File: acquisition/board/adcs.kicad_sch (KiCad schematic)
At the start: 111 parts, among them U1 AD9251, U2 XC7A50T-1FTG256C, U3 AD9251, U4 AD9251, U5 AD9251, U6 ICE40UP5K_QFN48

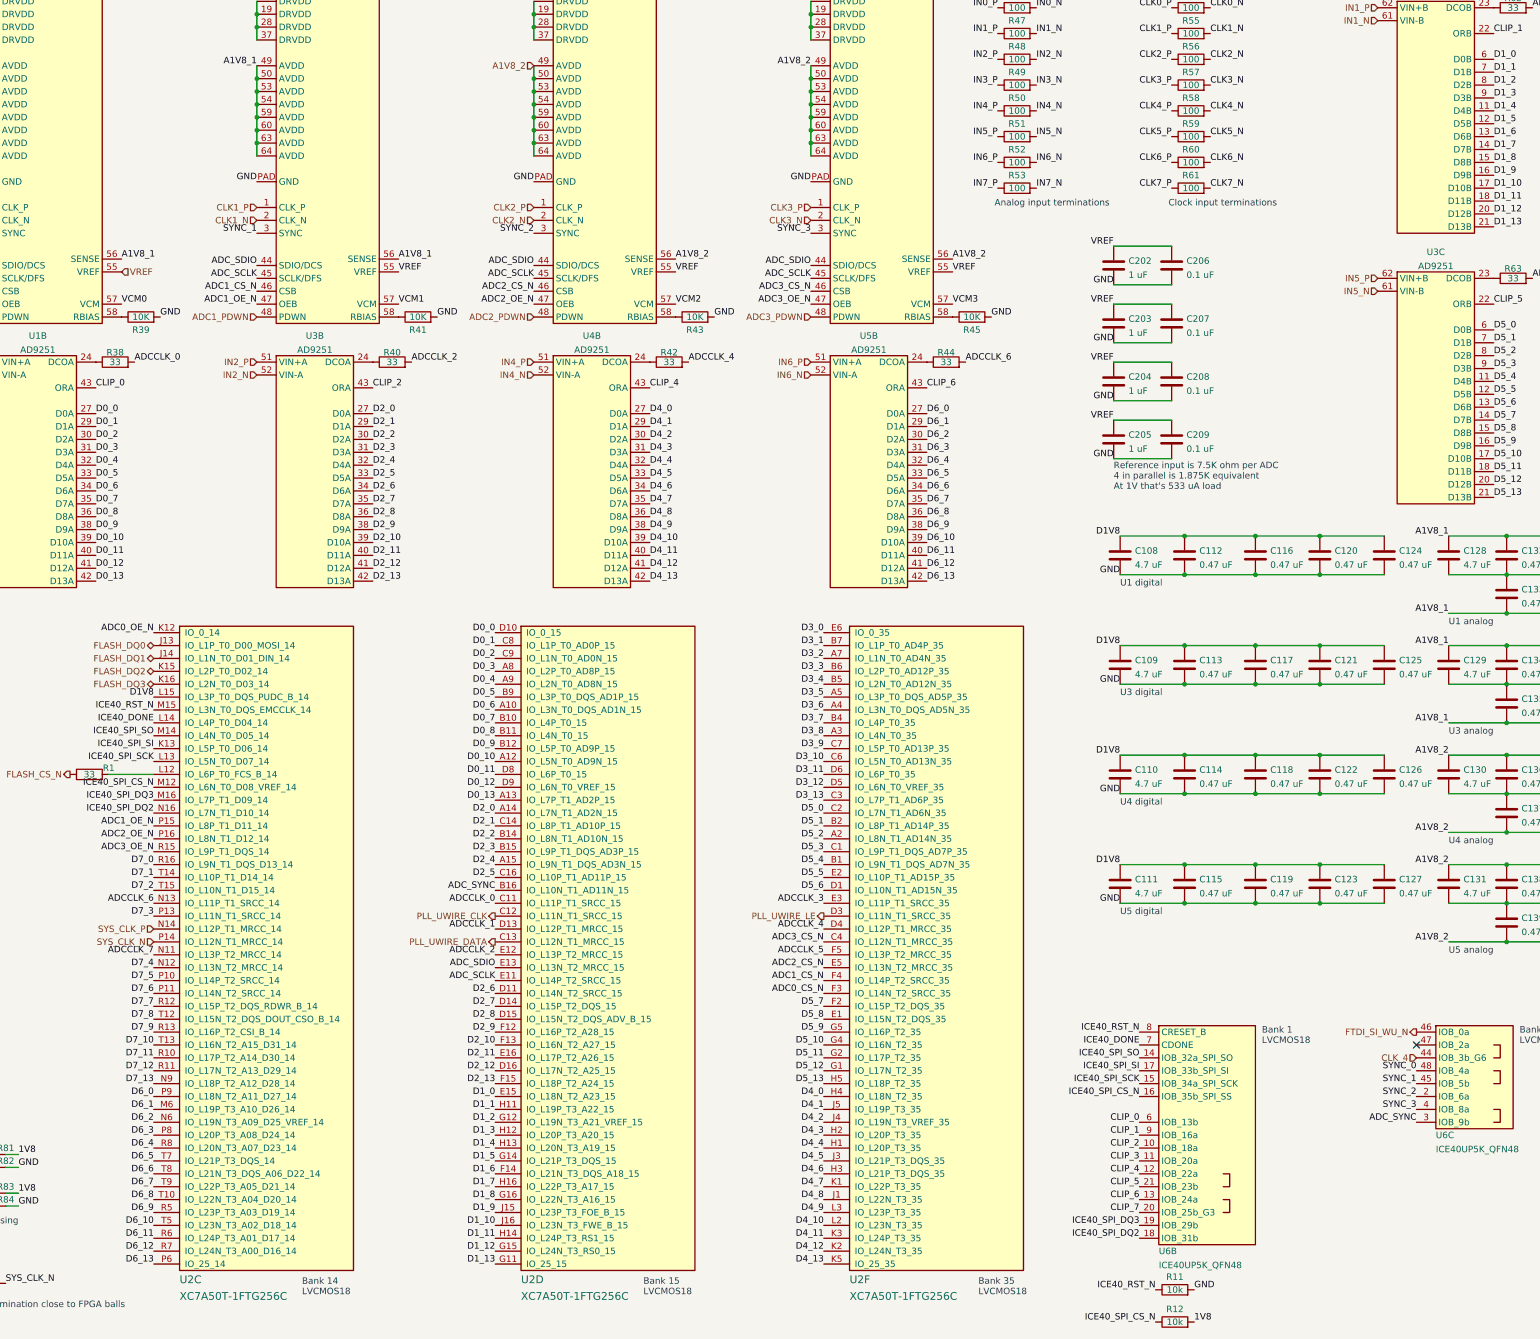
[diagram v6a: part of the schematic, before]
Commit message: Finished initial routing of RAM, hooked up almost all of first ADC
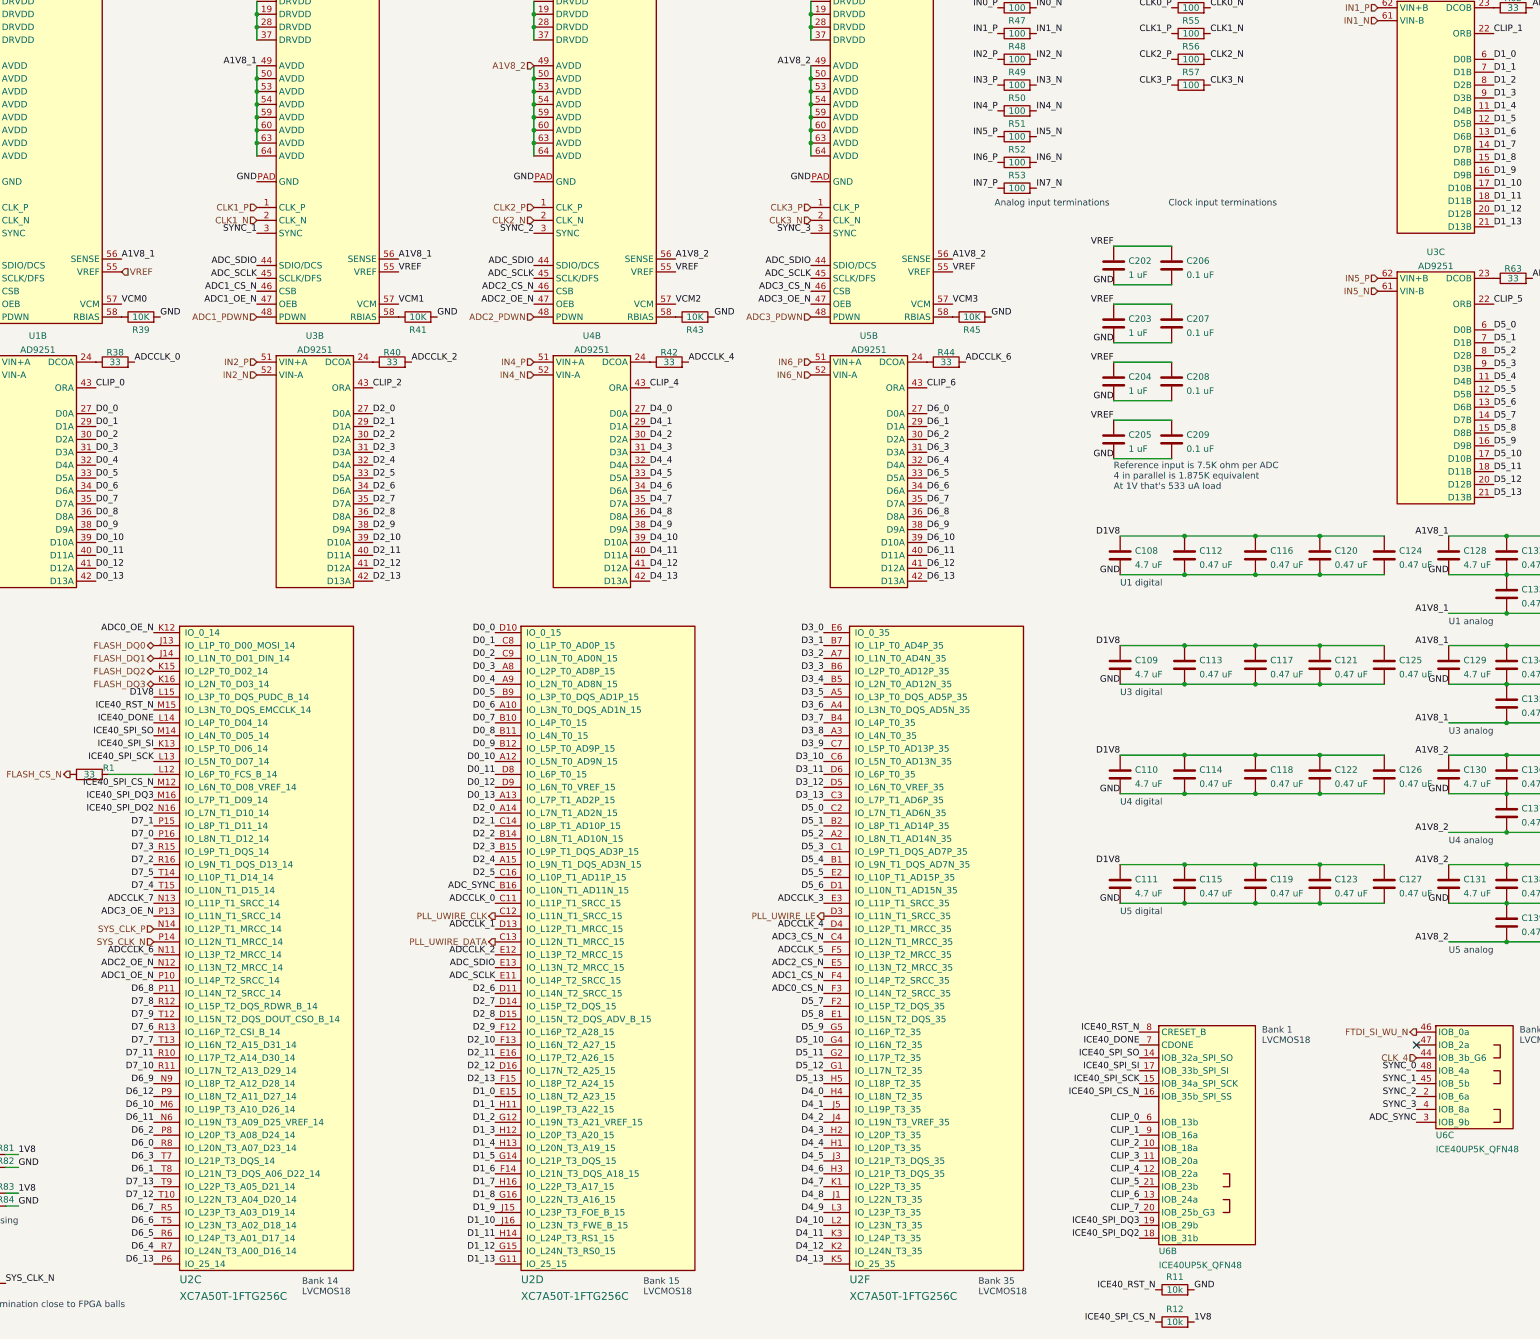
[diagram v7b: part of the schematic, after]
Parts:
- removed R58, R59, R60, R61: 100, azonenberg_pcb:EIA_0402_RES_NOSILK, symbol device:R
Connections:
- net ADC1_OE_N: now also U2.P10 (IO_L14P_T2_SRCC_14); no longer U2.P15 (IO_L8P_T1_D11_14)
- net ADC2_OE_N: now also U2.N12 (IO_L13N_T2_MRCC_14); no longer U2.P16 (IO_L8N_T1_D12_14)
- net ADC3_OE_N: now also U2.P13 (IO_L11N_T1_SRCC_14); no longer U2.R15 (IO_L9P_T1_DQS_14)
- net ADCCLK_6: now also U2.N11 (IO_L13P_T2_MRCC_14); no longer U2.N13 (IO_L11P_T1_SRCC_14)
- net ADCCLK_7: now also U2.N13 (IO_L11P_T1_SRCC_14); no longer U2.N11 (IO_L13P_T2_MRCC_14)
- net D6_0: now also U2.R8 (IO_L20N_T3_A07_D23_14); no longer U2.P9 (IO_L18N_T2_A11_D27_14)
- net D6_1: now also U2.T8 (IO_L21N_T3_DQS_A06_D22_14); no longer U2.M6 (IO_L19P_T3_A10_D26_14)
- net D6_10: now also U2.M6 (IO_L19P_T3_A10_D26_14); no longer U2.T5 (IO_L23N_T3_A02_D18_14)
- net D6_11: now also U2.N6 (IO_L19N_T3_A09_D25_VREF_14); no longer U2.R6 (IO_L24P_T3_A01_D17_14)
- net D6_12: now also U2.P9 (IO_L18N_T2_A11_D27_14); no longer U2.R7 (IO_L24N_T3_A00_D16_14)
- net D6_2: now also U2.P8 (IO_L20P_T3_A08_D24_14); no longer U2.N6 (IO_L19N_T3_A09_D25_VREF_14)
- net D6_3: now also U2.T7 (IO_L21P_T3_DQS_14); no longer U2.P8 (IO_L20P_T3_A08_D24_14)
- net D6_4: now also U2.R7 (IO_L24N_T3_A00_D16_14); no longer U2.R8 (IO_L20N_T3_A07_D23_14)
- net D6_5: now also U2.R6 (IO_L24P_T3_A01_D17_14); no longer U2.T7 (IO_L21P_T3_DQS_14)
- net D6_6: now also U2.T5 (IO_L23N_T3_A02_D18_14); no longer U2.T8 (IO_L21N_T3_DQS_A06_D22_14)
- net D6_7: now also U2.R5 (IO_L23P_T3_A03_D19_14); no longer U2.T9 (IO_L22P_T3_A05_D21_14)
- net D6_8: now also U2.P11 (IO_L14N_T2_SRCC_14); no longer U2.T10 (IO_L22N_T3_A04_D20_14)
- net D6_9: now also U2.N9 (IO_L18P_T2_A12_D28_14); no longer U2.R5 (IO_L23P_T3_A03_D19_14)
- net D7_0: now also U2.P16 (IO_L8N_T1_D12_14); no longer U2.R16 (IO_L9N_T1_DQS_D13_14)
- net D7_1: now also U2.P15 (IO_L8P_T1_D11_14); no longer U2.T14 (IO_L10P_T1_D14_14)
- net D7_10: now also U2.R11 (IO_L17N_T2_A13_D29_14); no longer U2.T13 (IO_L16N_T2_A15_D31_14)
- net D7_12: now also U2.T10 (IO_L22N_T3_A04_D20_14); no longer U2.R11 (IO_L17N_T2_A13_D29_14)
- net D7_13: now also U2.T9 (IO_L22P_T3_A05_D21_14); no longer U2.N9 (IO_L18P_T2_A12_D28_14)
- net D7_2: now also U2.R16 (IO_L9N_T1_DQS_D13_14); no longer U2.T15 (IO_L10N_T1_D15_14)
- net D7_3: now also U2.R15 (IO_L9P_T1_DQS_14); no longer U2.P13 (IO_L11N_T1_SRCC_14)
- net D7_4: now also U2.T15 (IO_L10N_T1_D15_14); no longer U2.N12 (IO_L13N_T2_MRCC_14)
- net D7_5: now also U2.T14 (IO_L10P_T1_D14_14); no longer U2.P10 (IO_L14P_T2_SRCC_14)
- net D7_6: now also U2.R13 (IO_L16P_T2_CSI_B_14); no longer U2.P11 (IO_L14N_T2_SRCC_14)
- net D7_7: now also U2.T13 (IO_L16N_T2_A15_D31_14); no longer U2.R12 (IO_L15P_T2_DQS_RDWR_B_14)
- net D7_8: now also U2.R12 (IO_L15P_T2_DQS_RDWR_B_14); no longer U2.T12 (IO_L15N_T2_DQS_DOUT_CSO_B_14)
- net D7_9: now also U2.T12 (IO_L15N_T2_DQS_DOUT_CSO_B_14); no longer U2.R13 (IO_L16P_T2_CSI_B_14)
- net GND: now also C128.2, C129.2, C130.2, C131.2, C132.2, C133.1, C134.2, C135.1, C136.2, C137.1, C138.2, C139.1, C140.2, C141.1, C142.2, C143.1, C144.2, C145.1, C146.2, C147.1, C148.2, C149.1, C150.2, C151.1, C152.2, C153.1, C154.2, C155.1, C156.2, C157.1, C158.2, C159.1, C160.2, C161.1, C162.2, C163.1

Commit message: Continued layout of bottom ADC, routed FPGA JTAG
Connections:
- net 1V8: no longer R81.1, R83.1
- net ADC1_OE_N: now also U2.C4 (IO_L12N_T1_MRCC_35); no longer U2.P10 (IO_L14P_T2_SRCC_14)
- net ADC2_OE_N: now also U2.M12 (IO_L6N_T0_D08_VREF_14); no longer U2.N12 (IO_L13N_T2_MRCC_14)
- net ADC3_CS_N: now also U2.P6 (IO_25_14); no longer U2.C4 (IO_L12N_T1_MRCC_35)
- net ADC3_OE_N: now also U2.N6 (IO_L19N_T3_A09_D25_VREF_14); no longer U2.P13 (IO_L11N_T1_SRCC_14)
- net ADC_SCLK: now also U2.N12 (IO_L13N_T2_MRCC_14); no longer U2.E11 (IO_L14P_T2_SRCC_15)
- net ADC_SDIO: now also U2.M6 (IO_L19P_T3_A10_D26_14); no longer U2.E13 (IO_L13N_T2_MRCC_15)
- net D1V8: now also R81.1, R83.1
- net D6_10: now also U2.P11 (IO_L14N_T2_SRCC_14); no longer U2.M6 (IO_L19P_T3_A10_D26_14)
- net D6_11: now also U2.P9 (IO_L18N_T2_A11_D27_14); no longer U2.N6 (IO_L19N_T3_A09_D25_VREF_14)
- net D6_12: now also U2.M14 (IO_L4N_T0_D05_14); no longer U2.P9 (IO_L18N_T2_A11_D27_14)
- net D6_13: now also U2.N9 (IO_L18P_T2_A12_D28_14); no longer U2.P6 (IO_25_14)
- net D6_8: now also U2.P13 (IO_L11N_T1_SRCC_14); no longer U2.P11 (IO_L14N_T2_SRCC_14)
- net D6_9: now also U2.P10 (IO_L14P_T2_SRCC_14); no longer U2.N9 (IO_L18P_T2_A12_D28_14)
- net ICE40_SPI_CS_N: now also U2.E13 (IO_L13N_T2_MRCC_15); no longer U2.M12 (IO_L6N_T0_D08_VREF_14)
- net ICE40_SPI_SO: now also U2.E11 (IO_L14P_T2_SRCC_15); no longer U2.M14 (IO_L4N_T0_D05_14)
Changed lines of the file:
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@@
   (title_block
     (title "Digitizer board")
-    (date "2023-01-29")
+    (date "2023-01-31")
     (rev "0.1")
     (company "A. Zonenberg")
@@
     (effects (font (size 1.27 1.27)) (justify right bottom))
   )
-  (label "D6_9" (at 63.5 236.22 180)
+  (label "D6_9" (at 63.5 215.9 180)
     (effects (font (size 1.27 1.27)) (justify right bottom))
   )
@@
     (effects (font (size 1.27 1.27)) (justify right bottom))
   )
-  (label "ICE40_SPI_SO" (at 63.5 167.64 180)
+  (label "ICE40_SPI_SO" (at 130.81 215.9 180)
     (effects (font (size 1.27 1.27)) (justify right bottom))
   )
@@
     (effects (font (size 1.27 1.27)) (justify left bottom))
   )
-  (label "ADC2_OE_N" (at 63.5 213.36 180)
+  (label "ADC2_OE_N" (at 63.5 177.8 180)
     (effects (font (size 1.27 1.27)) (justify right bottom))
   )
@@
     (effects (font (size 1.27 1.27)) (justify right bottom))
   )
-  (label "ADC_SDIO" (at 130.81 213.36 180)
+  (label "ADC_SDIO" (at 63.5 241.3 180)
     (effects (font (size 1.27 1.27)) (justify right bottom))
   )
@@
     (effects (font (size 1.27 1.27)) (justify right bottom))
   )
-  (label "ADC3_CS_N" (at 195.58 208.28 180)
+  (label "ADC3_CS_N" (at 63.5 271.78 180)
     (effects (font (size 1.27 1.27)) (justify right bottom))
   )
@@
     (effects (font (size 1.27 1.27)) (justify right bottom))
   )
-  (label "1V8" (at 36.83 257.81 0)
+  (label "D1V8" (at 36.83 257.81 0)
     (effects (font (size 1.27 1.27)) (justify left bottom))
   )
@@
     (effects (font (size 1.27 1.27)) (justify right bottom))
   )
-  (label "1V8" (at 36.83 250.19 0)
+  (label "D1V8" (at 36.83 250.19 0)
     (effects (font (size 1.27 1.27)) (justify left bottom))
   )
@@
     (effects (font (size 1.27 1.27)) (justify right bottom))
   )
-  (label "ADC3_OE_N" (at 63.5 203.2 180)
+  (label "ADC3_OE_N" (at 63.5 243.84 180)
     (effects (font (size 1.27 1.27)) (justify right bottom))
   )
@@
     (effects (font (size 1.27 1.27)) (justify left bottom))
   )
-  (label "ICE40_SPI_CS_N" (at 63.5 177.8 180)
+  (label "ICE40_SPI_CS_N" (at 130.81 213.36 180)
     (effects (font (size 1.27 1.27)) (justify right bottom))
   )
@@
     (effects (font (size 1.27 1.27)) (justify right bottom))
   )
-  (label "D6_12" (at 63.5 238.76 180)
+  (label "D6_12" (at 63.5 167.64 180)
     (effects (font (size 1.27 1.27)) (justify right bottom))
   )
@@
     (effects (font (size 1.27 1.27)) (justify left bottom))
   )
-  (label "D6_10" (at 63.5 241.3 180)
+  (label "D6_10" (at 63.5 218.44 180)
     (effects (font (size 1.27 1.27)) (justify right bottom))
   )
@@
     (effects (font (size 1.27 1.27)) (justify left bottom))
   )
-  (label "ADC_SCLK" (at 130.81 215.9 180)
+  (label "ADC_SCLK" (at 63.5 213.36 180)
     (effects (font (size 1.27 1.27)) (justify right bottom))
   )
@@
     (effects (font (size 1.27 1.27)) (justify right bottom))
   )
-  (label "D6_11" (at 63.5 243.84 180)
+  (label "D6_11" (at 63.5 238.76 180)
     (effects (font (size 1.27 1.27)) (justify right bottom))
   )
@@
     (effects (font (size 1.27 1.27)) (justify right bottom))
   )
-  (label "ADC1_OE_N" (at 63.5 215.9 180)
+  (label "ADC1_OE_N" (at 195.58 208.28 180)
     (effects (font (size 1.27 1.27)) (justify right bottom))
   )
@@
     (effects (font (size 1.27 1.27)) (justify right bottom))
   )
-  (label "D6_13" (at 63.5 271.78 180)
+  (label "D6_13" (at 63.5 236.22 180)
     (effects (font (size 1.27 1.27)) (justify right bottom))
   )
@@
     (effects (font (size 1.27 1.27)) (justify left bottom))
   )
-  (label "D6_8" (at 63.5 218.44 180)
-    (effects (font (size 1.27 1.27)) (justify right bottom))
-  )
+  (label "D6_8" (at 63.5 203.2 180)
+    (effects (font (size 1.27 1.27)) (justify right bottom))
+  )
